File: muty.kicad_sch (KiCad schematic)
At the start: 0 parts

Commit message: feat: add bq25887 connector
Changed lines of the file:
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@@
 	(paper "A4")
 	(sheet
-		(at 0 0)
+		(at -325.12 214.63)
 		(size 297.18 209.55)
 		(exclude_from_sim no)
@@
 		)
 		(property "Sheetname" "muty_BQ25887RGE"
-			(at 0 -0.7116 0)
+			(at -325.12 213.9184 0)
 			(effects
 				(font
@@
 		)
 		(property "Sheetfile" "power.kicad_sch"
-			(at 0 210.1346 0)
+			(at -325.12 424.7646 0)
 			(effects
 				(font

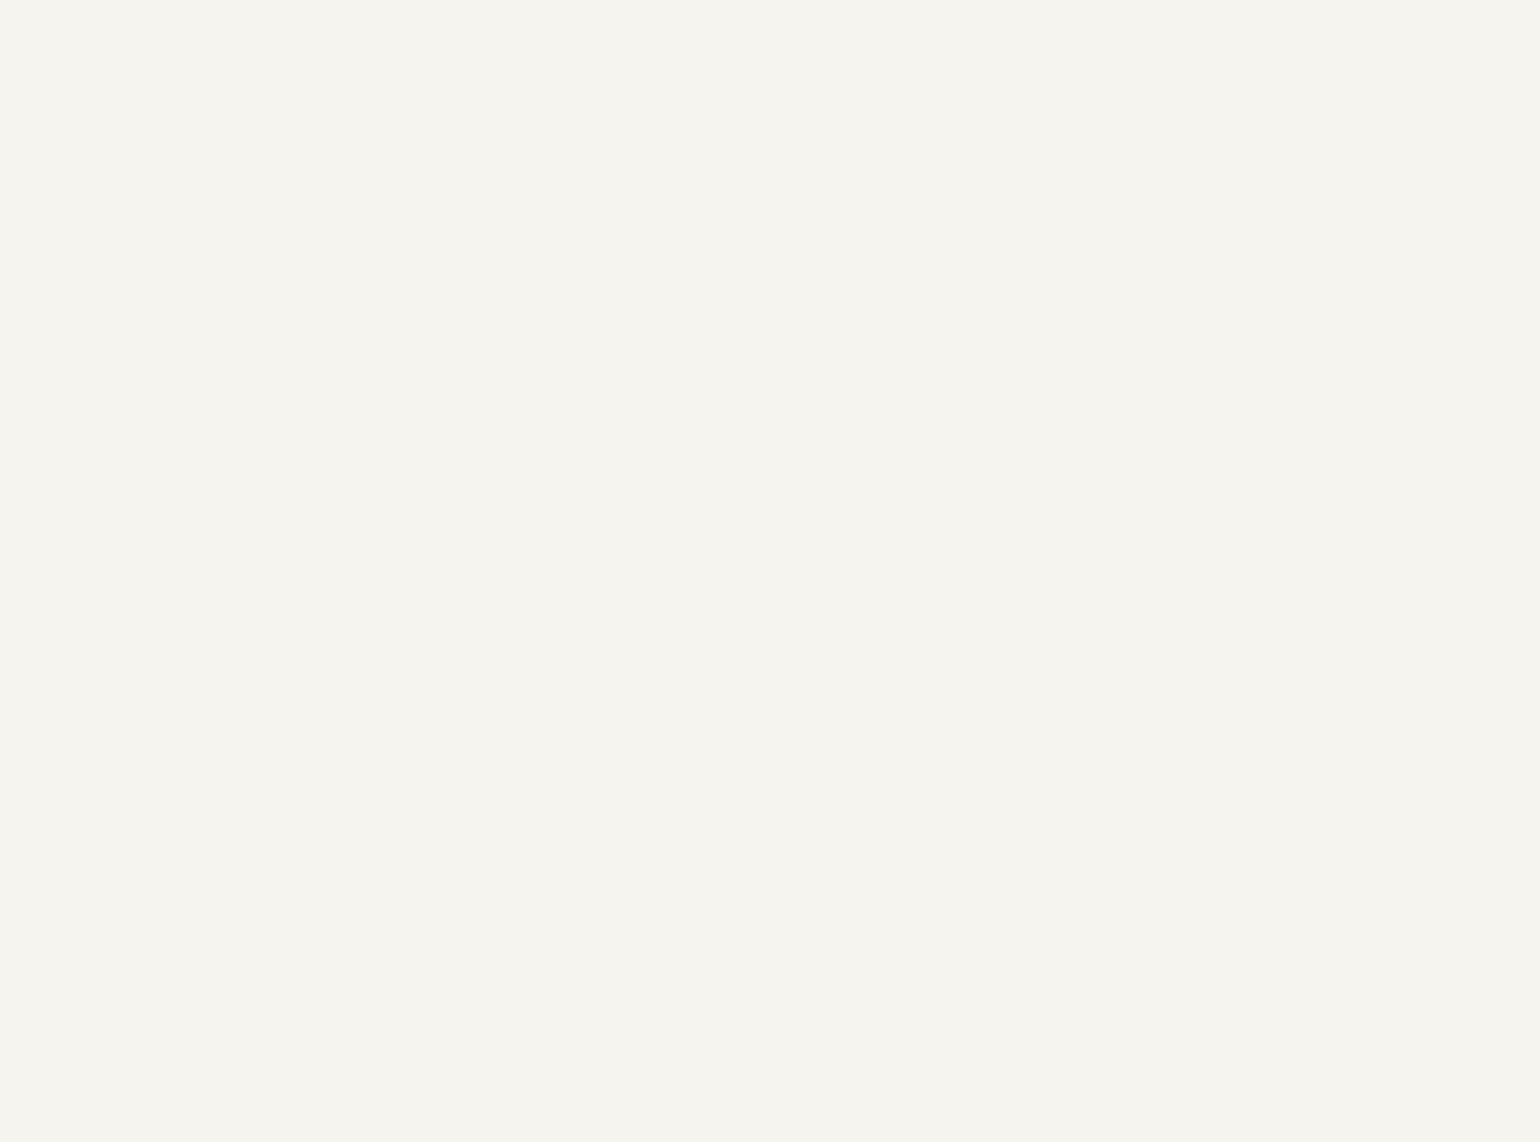
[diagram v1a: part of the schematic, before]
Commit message: feat: add bno085+bme280
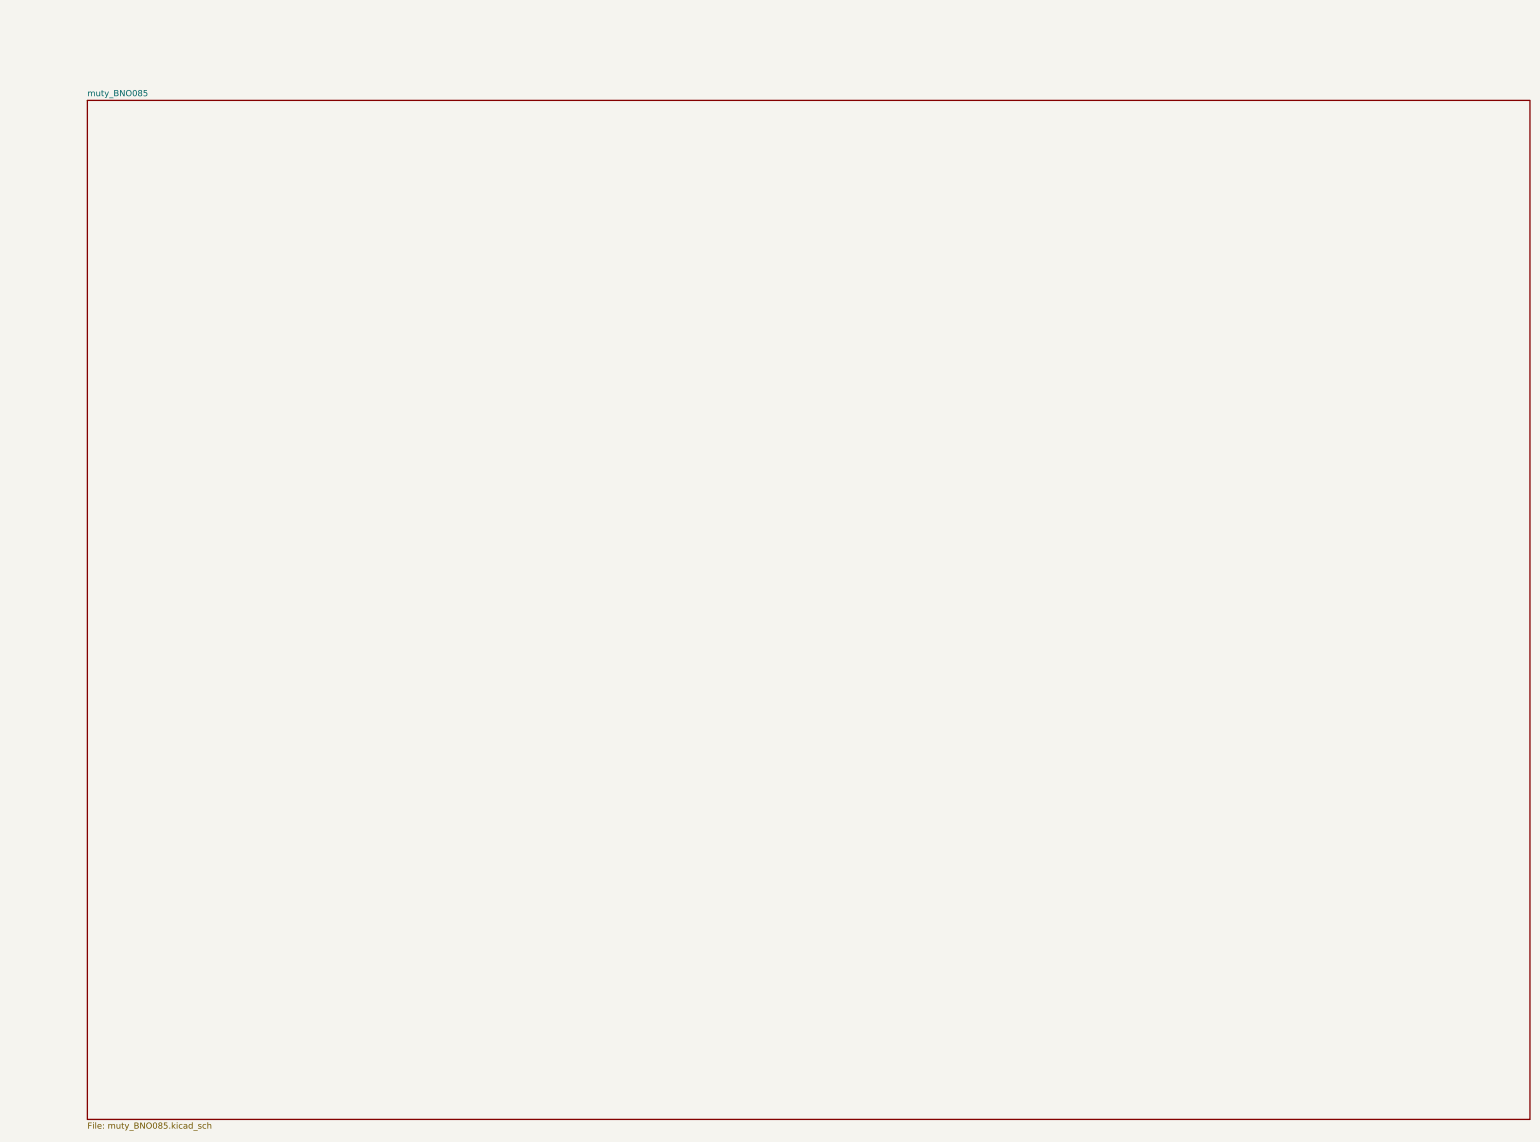
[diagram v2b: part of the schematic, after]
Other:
- added sheet muty_BNO085 (muty_BNO085.kicad_sch)
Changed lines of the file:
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@@
 	(paper "A4")
+	(sheet
+		(at 1.27 214.63)
+		(size 298.45 210.82)
+		(exclude_from_sim no)
+		(in_bom yes)
+		(on_board yes)
+		(dnp no)
+		(fields_autoplaced yes)
+		(stroke
+			(width 0.1524)
+			(type solid)
+		)
+		(fill
+			(color 0 0 0 0.0000)
+		)
+		(property "Sheetname" "muty_BNO085"
+			(at 1.27 213.9184 0)
+			(effects
+				(font
+					(size 1.27 1.27)
+				)
+				(justify left bottom)
+			)
+		)
+		(property "Sheetfile" "muty_BNO085.kicad_sch"
+			(at 1.27 426.0346 0)
+			(effects
+				(font
+					(size 1.27 1.27)
+				)
+				(justify left top)
+			)
+		)
+		(instances
+			(project "muty"
+				(path "/c2c8c614-99fc-45e9-8585-8c2a223a7e3c"
+					(page "4")
+				)
+			)
+		)
+	)
 	(sheet
 		(at -325.12 214.63)

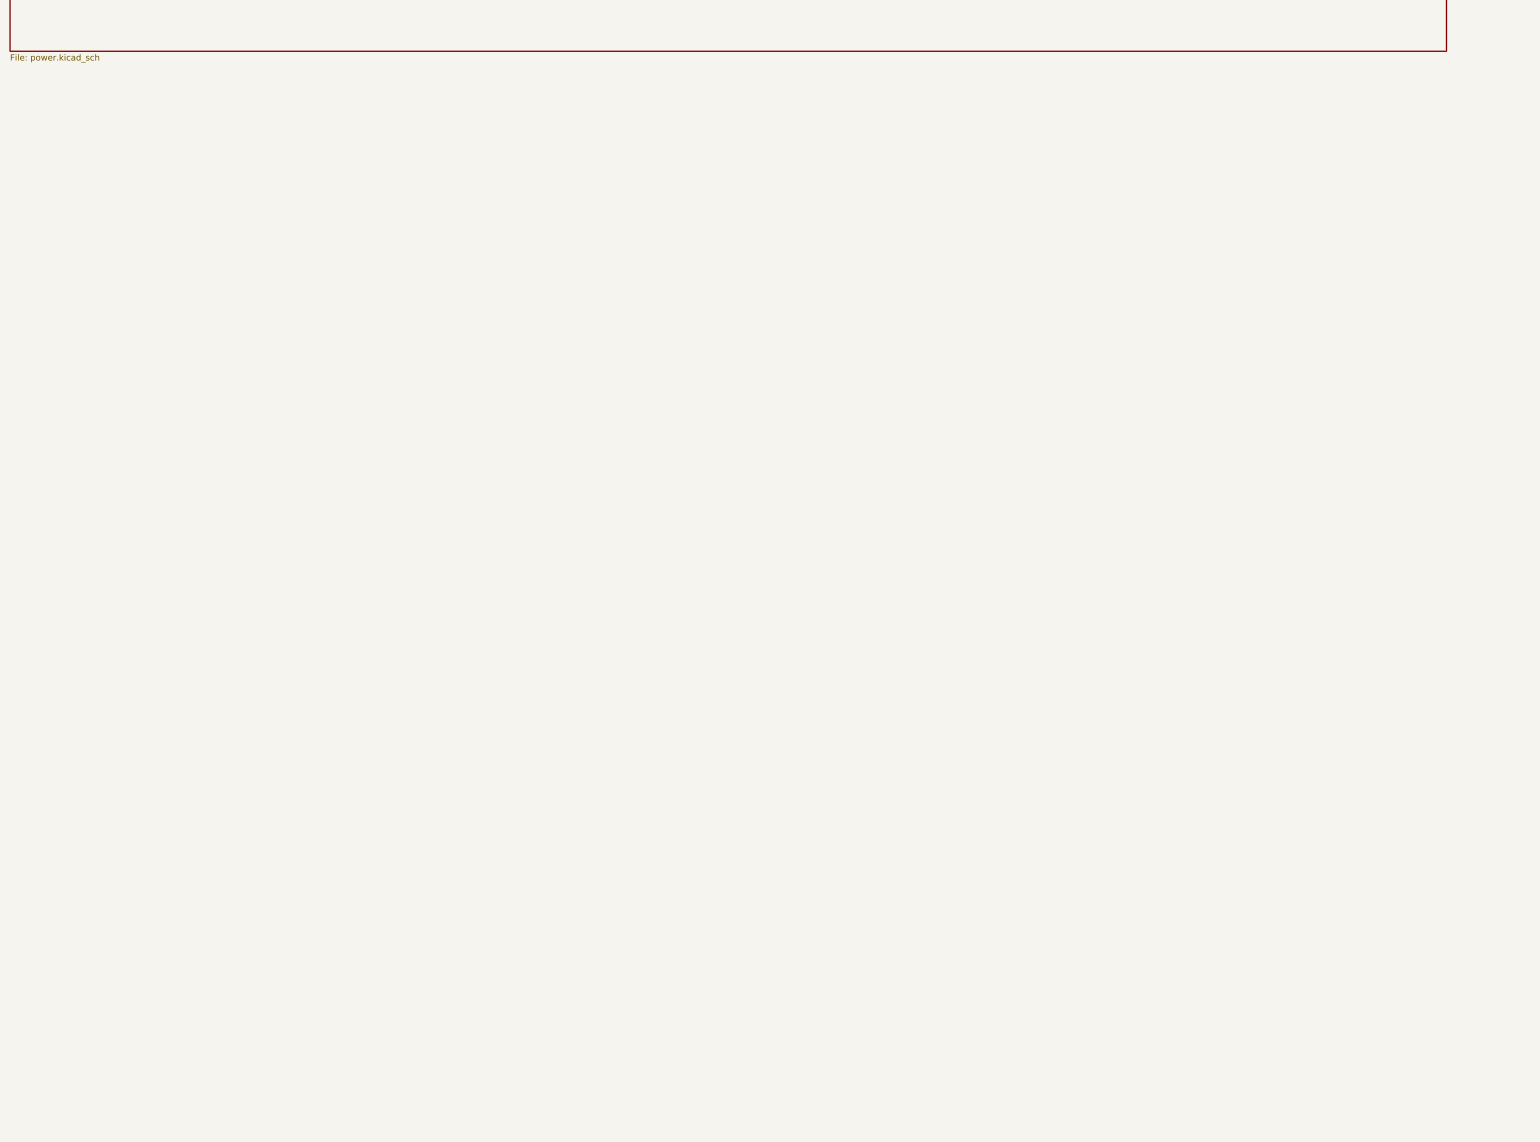
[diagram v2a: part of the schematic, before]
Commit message: feat: add tb6612fng
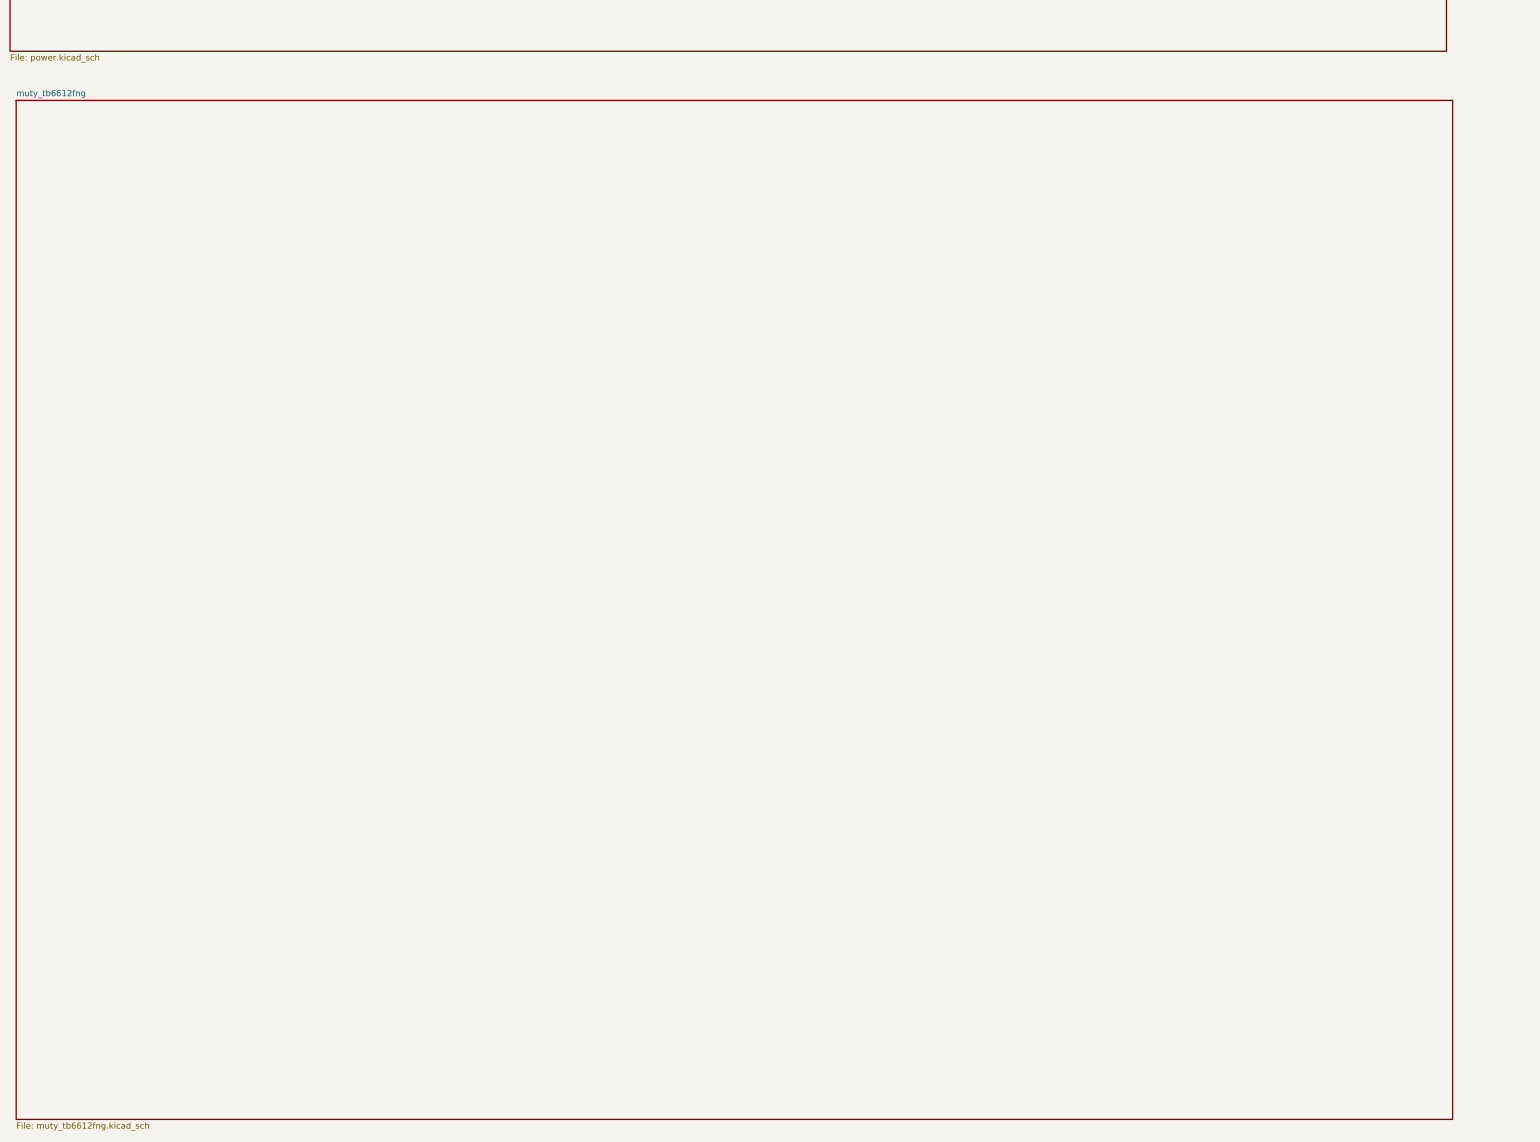
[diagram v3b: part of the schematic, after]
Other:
- added sheet muty_tb6612fng (muty_tb6612fng.kicad_sch)
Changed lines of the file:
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@@
 	(paper "A4")
+	(sheet
+		(at -323.85 434.34)
+		(size 297.18 210.82)
+		(exclude_from_sim no)
+		(in_bom yes)
+		(on_board yes)
+		(dnp no)
+		(fields_autoplaced yes)
+		(stroke
+			(width 0.1524)
+			(type solid)
+		)
+		(fill
+			(color 0 0 0 0.0000)
+		)
+		(property "Sheetname" "muty_tb6612fng"
+			(at -323.85 433.6284 0)
+			(effects
+				(font
+					(size 1.27 1.27)
+				)
+				(justify left bottom)
+			)
+		)
+		(property "Sheetfile" "muty_tb6612fng.kicad_sch"
+			(at -323.85 645.7446 0)
+			(effects
+				(font
+					(size 1.27 1.27)
+				)
+				(justify left top)
+			)
+		)
+		(instances
+			(project "muty"
+				(path "/c2c8c614-99fc-45e9-8585-8c2a223a7e3c"
+					(page "5")
+				)
+			)
+		)
+	)
 	(sheet
 		(at 1.27 214.63)

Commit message: feat: add ethernet
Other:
- added sheet muty_VL53L0X (muty_VL53L0X.kicad_sch)
- added sheet muty_ethernet (muty_ethernet.kicad_sch)
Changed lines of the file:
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@@
+	)
+	(sheet
+		(at -322.58 659.13)
+		(size 297.18 210.82)
+		(exclude_from_sim no)
+		(in_bom yes)
+		(on_board yes)
+		(dnp no)
+		(fields_autoplaced yes)
+		(stroke
+			(width 0.1524)
+			(type solid)
+		)
+		(fill
+			(color 0 0 0 0.0000)
+		)
+		(property "Sheetname" "muty_ethernet"
+			(at -322.58 658.4184 0)
+			(effects
+				(font
+					(size 1.27 1.27)
+				)
+				(justify left bottom)
+			)
+		)
+		(property "Sheetfile" "muty_ethernet.kicad_sch"
+			(at -322.58 870.5346 0)
+			(effects
+				(font
+					(size 1.27 1.27)
+				)
+				(justify left top)
+			)
+		)
+		(instances
+			(project "muty"
+				(path "/c2c8c614-99fc-45e9-8585-8c2a223a7e3c"
+					(page "7")
+				)
+			)
+		)
+	)
+	(sheet
+		(at 1.27 434.34)
+		(size 297.18 210.82)
+		(exclude_from_sim no)
+		(in_bom yes)
+		(on_board yes)
+		(dnp no)
+		(fields_autoplaced yes)
+		(stroke
+			(width 0.1524)
+			(type solid)
+		)
+		(fill
+			(color 0 0 0 0.0000)
+		)
+		(property "Sheetname" "muty_VL53L0X"
+			(at 1.27 433.6284 0)
+			(effects
+				(font
+					(size 1.27 1.27)
+				)
+				(justify left bottom)
+			)
+		)
+		(property "Sheetfile" "muty_VL53L0X.kicad_sch"
+			(at 1.27 645.7446 0)
+			(effects
+				(font
+					(size 1.27 1.27)
+				)
+				(justify left top)
+			)
+		)
+		(instances
+			(project "muty"
+				(path "/c2c8c614-99fc-45e9-8585-8c2a223a7e3c"
+					(page "6")
+				)
+			)
+		)
 	)
 	(sheet
